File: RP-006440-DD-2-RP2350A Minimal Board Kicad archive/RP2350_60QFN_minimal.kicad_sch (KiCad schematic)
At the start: 45 parts, among them J1 USB_C_Receptacle_USB2.0_16P, J2 Conn_02x18_Odd_Even, J3 Conn_02x18_Odd_Even, J4 SM03B-SRSS-TB, SW1 SW_Push, SW2 SW_Push, U1 RP2350_60QFN, U2 NCP1117-3.3_SOT223, U3 W25Q128JVS, Y1 ABM8-272-T3

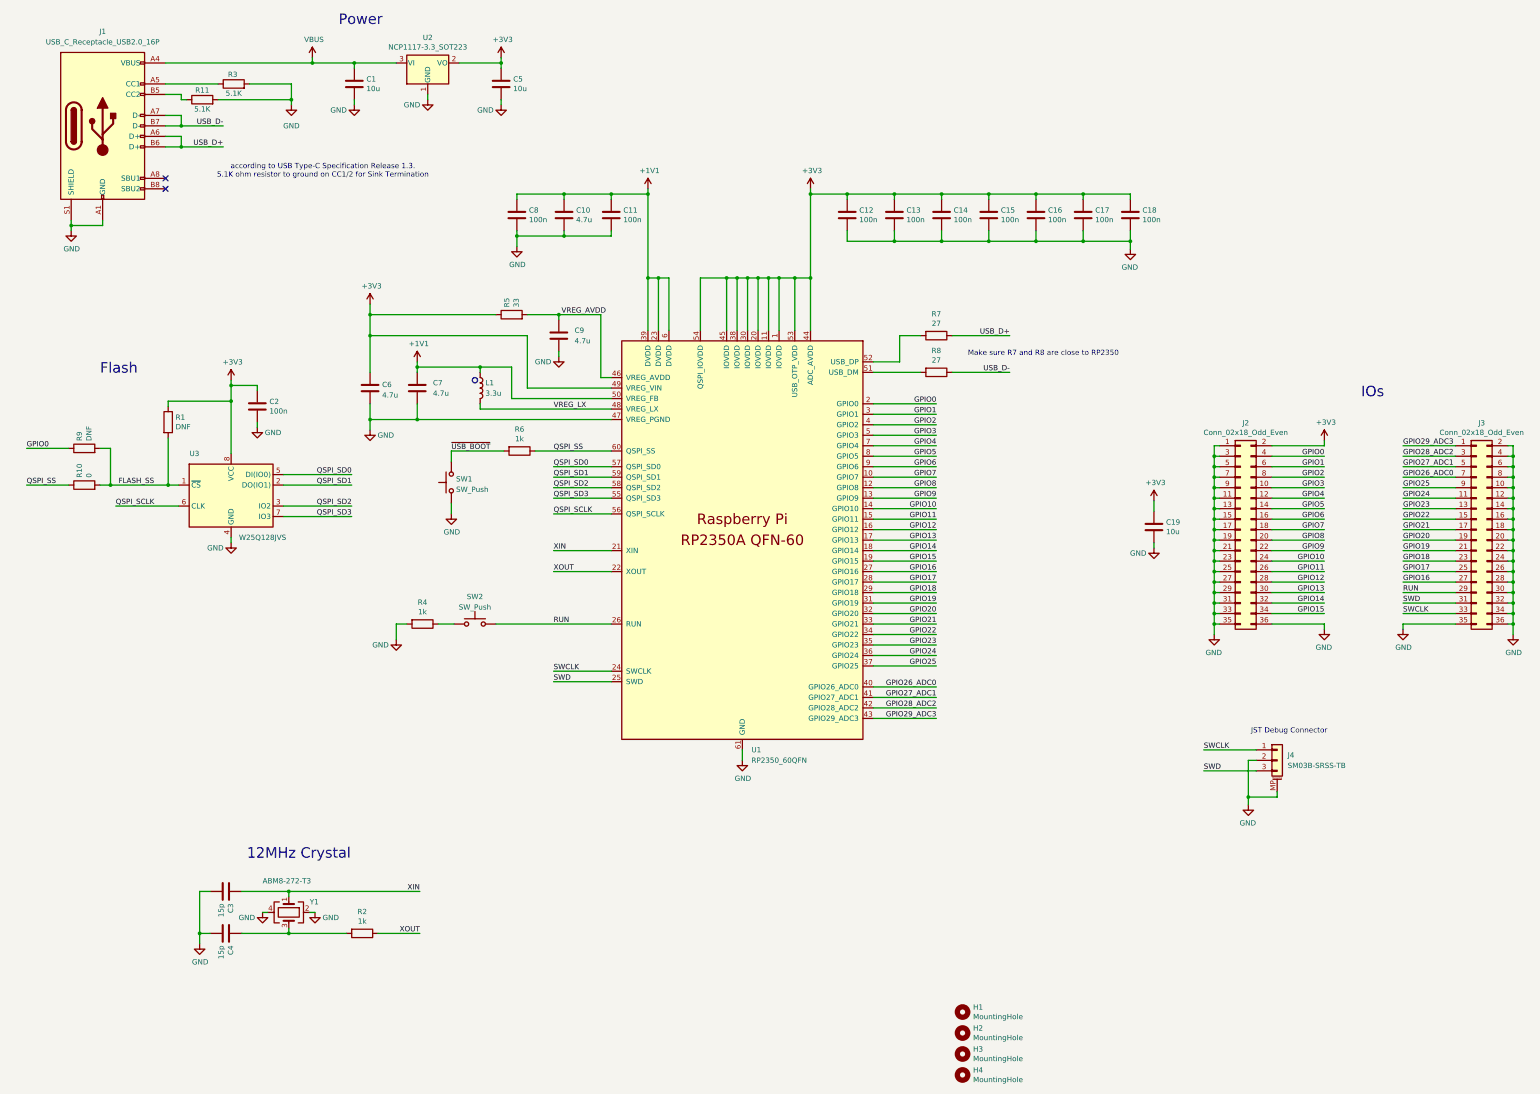
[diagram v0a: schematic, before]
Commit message: Added secondary memory to schematic
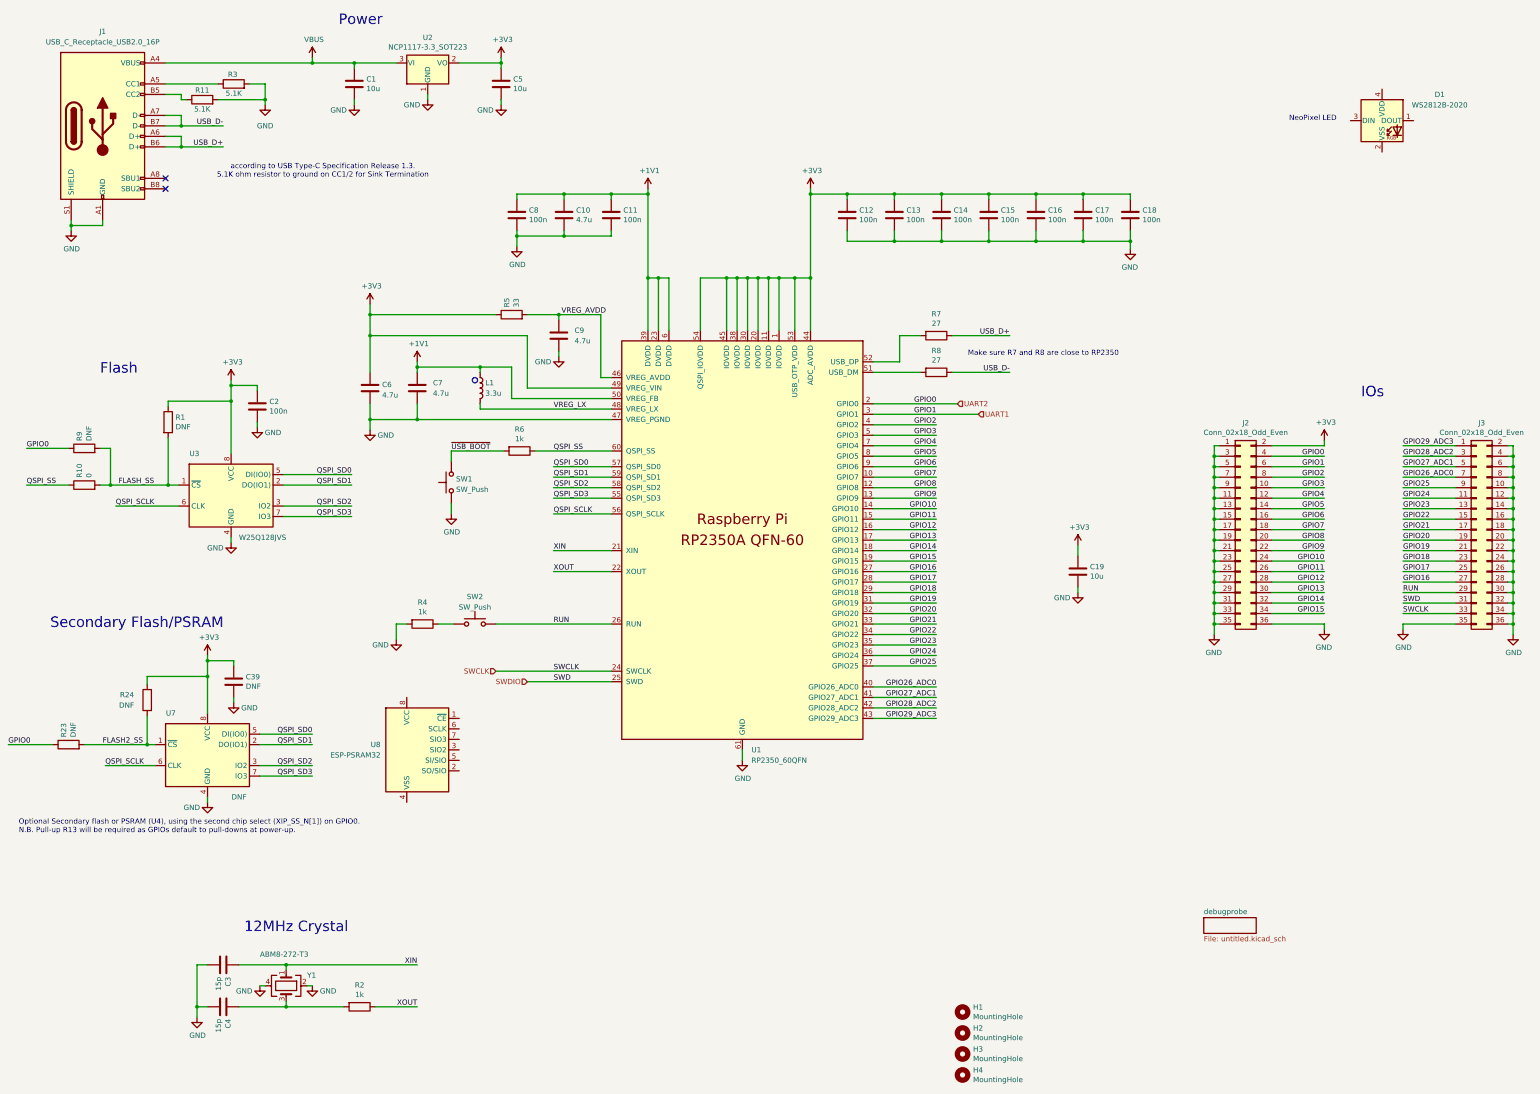
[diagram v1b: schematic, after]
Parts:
- removed J4: SM03B-SRSS-TB, Connector_JST:JST_SH_SM03B-SRSS-TB_1x03-1MP_P1.00mm_Horizontal, symbol Connector_Generic_MountingPin:Conn_01x03_MountingPin
- added C39: DNF, Capacitor_SMD:C_0402_1005Metric, symbol Device:C
- added D1: WS2812B-2020, LED_SMD:LED_WS2812B-2020_PLCC4_2.0x2.0mm, symbol LED:WS2812B-2020
- added R23, R24: DNF, Resistor_SMD:R_0402_1005Metric, symbol Device:R
- added U7: DNF, Package_SO:SOIC-8_5.23x5.23mm_P1.27mm, symbol Memory_Flash:W25Q128JVS
- added U8: ESP-PSRAM32, Package_SO:SOIC-8_3.9x4.9mm_P1.27mm, symbol Memory_RAM:ESP-PSRAM32
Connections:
- net +3V3: now also C39.1, R24.1, U7.8 (VCC)
- net GND: now also C39.2, U7.4 (GND)
- net QSPI_SCLK: now also U7.6 (CLK)
- net QSPI_SD0: now also U7.5 (DI(IO0))
- net QSPI_SD1: now also U7.2 (DO(IO1))
- net QSPI_SD2: now also U7.3 (IO2)
- net QSPI_SD3: now also U7.7 (IO3)
- net GPIO0 renamed UART2
- net UART2: now also R23.1
- net GPIO1 renamed UART1
- net SWD renamed SWDIO
- new net FLASH2_SS: R23.2, R24.2, U7.1 (~{CS})
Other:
- added sheet debugprobe (untitled.kicad_sch)
- note added: "NeoPixel LED"
- note added: "Optional Secondary flash or PSRAM (U4), using the second chip select (XIP_SS_N[1]) on GPIO0. N.B. Pull-up R13 will be required as GPIOs default to pull-downs at power-up."
- note added: "Secondary Flash/PSRAM"
- note removed: "JST Debug Connector"
- moved on the sheet: C19, C3, C4, R2, Y1
